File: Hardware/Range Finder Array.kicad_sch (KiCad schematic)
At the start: 8 parts

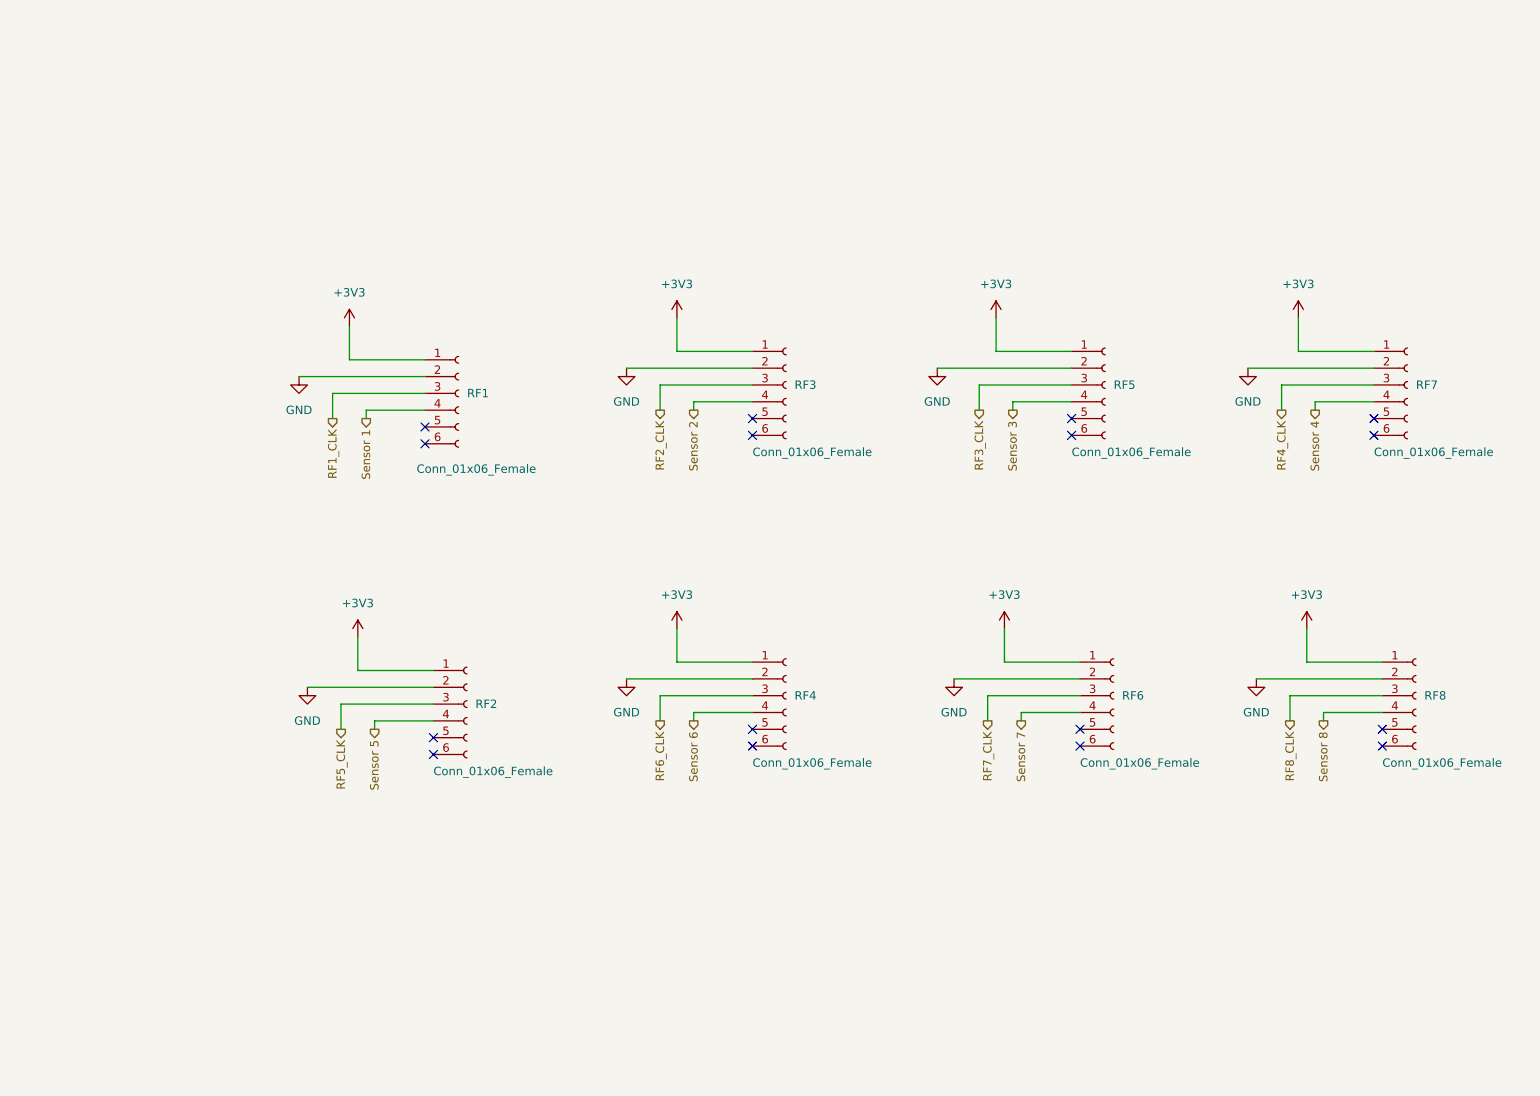
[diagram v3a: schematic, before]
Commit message: Add VL53L0X
Added VL53L0X range finders and reworked traces.
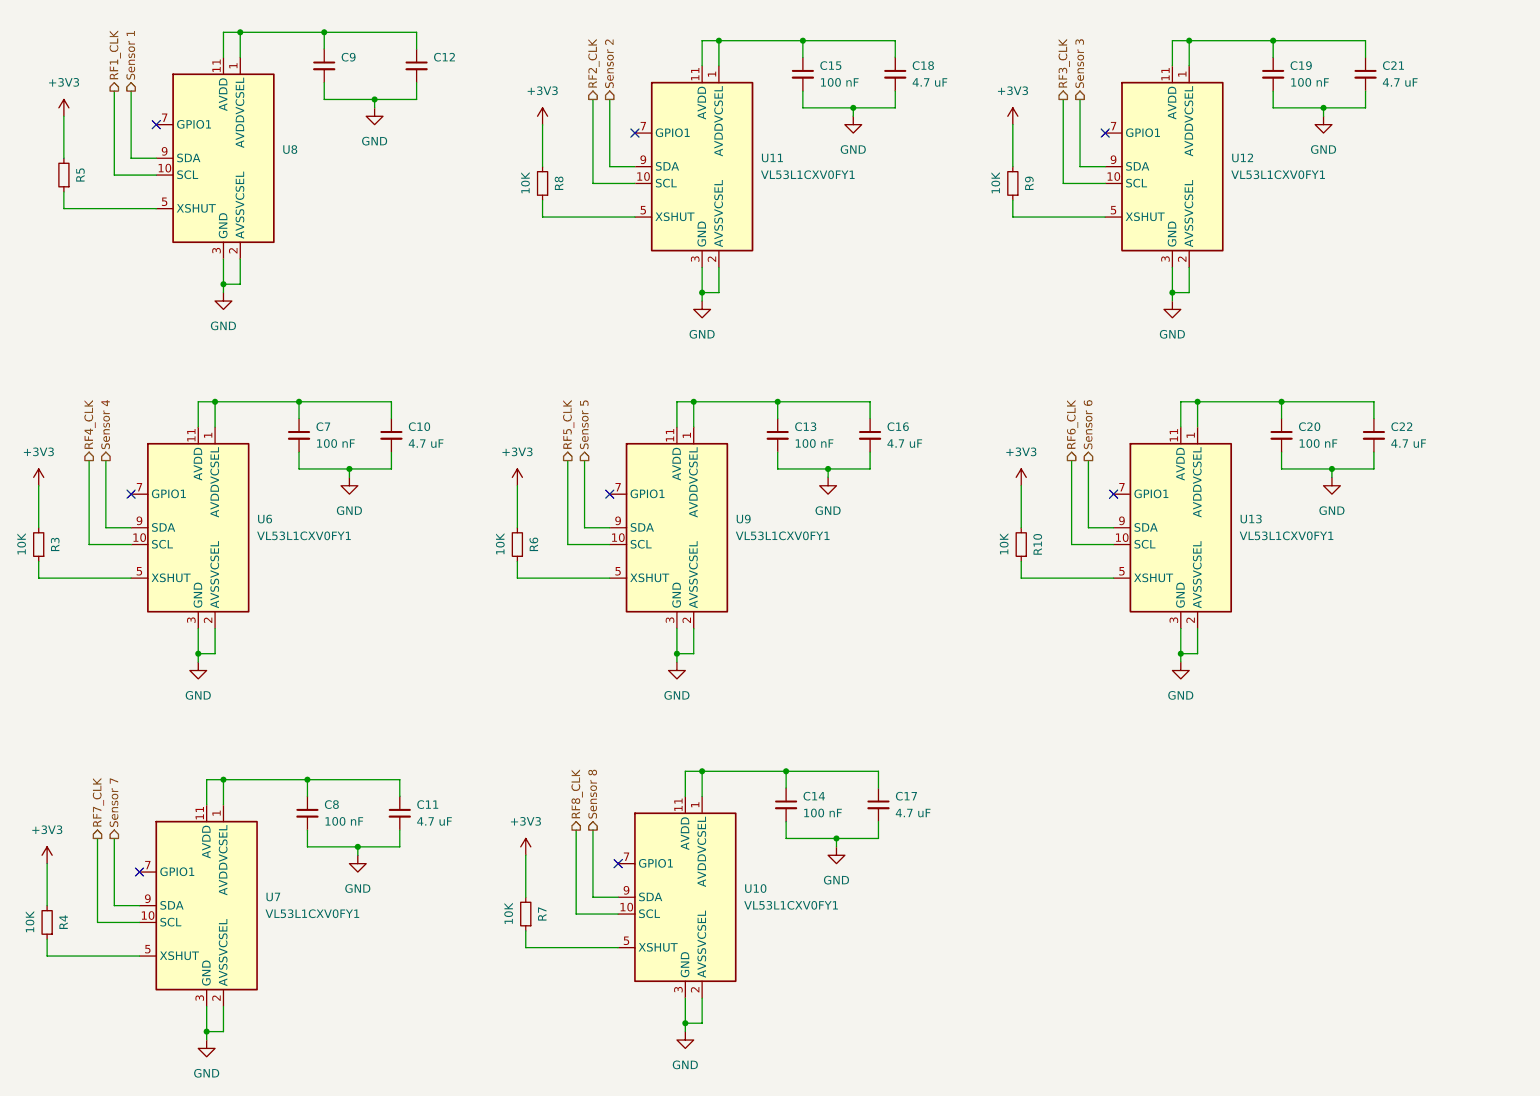
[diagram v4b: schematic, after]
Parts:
- removed RF1, RF2, RF3, RF4, RF5, RF6, RF7, RF8: Conn_01x06_Female, Connector_PinHeader_2.54mm:PinHeader_1x06_P2.54mm_Vertical, symbol Connector:Conn_01x06_Female
- added C10, C11, C16, C17, C18, C21, C22: 4.7 uF, Capacitor_SMD:C_0805_2012Metric, symbol Device:C_Small
- added C12, C9: (no value), symbol Device:C_Small
- added C13, C14, C15, C19, C20, C7, C8: 100 nF, Capacitor_SMD:C_0805_2012Metric, symbol Device:C_Small
- added R10, R3, R4, R6, R7, R8, R9: 10K, Resistor_SMD:R_0805_2012Metric, symbol Device:R_Small
- added R5: (no value), symbol Device:R_Small
- added U10, U11, U12, U13, U6, U7, U9: VL53L1CXV0FY1, Sensor_Distance:ST_VL53L1x, symbol Sensor_Distance:VL53L1CXV0FY1
- added U8: (no value), symbol Sensor_Distance:VL53L1CXV0FY1
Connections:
- net +3V3: now also R10.2, R3.2, R4.2, R5.2, R6.2, R7.2, R8.2, R9.2
- net GND: now also C10.2, C11.2, C12.2, C13.2, C14.2, C15.2, C16.2, C17.2, C18.2, C19.2, C20.2, C21.2, C22.2, C7.2, C8.2, C9.2, U10.12 (GND), U10.2 (AVSSVCSEL), U10.3 (GND), U10.4 (GND), U10.6 (GND), U11.12 (GND), U11.2 (AVSSVCSEL), U11.3 (GND), U11.4 (GND), U11.6 (GND), U12.12 (GND), U12.2 (AVSSVCSEL), U12.3 (GND), U12.4 (GND), U12.6 (GND), U13.12 (GND), U13.2 (AVSSVCSEL), U13.3 (GND), U13.4 (GND), U13.6 (GND), U6.12 (GND), U6.2 (AVSSVCSEL), U6.3 (GND), U6.4 (GND), U6.6 (GND), U7.12 (GND), U7.2 (AVSSVCSEL), U7.3 (GND), U7.4 (GND), U7.6 (GND), U8.12 (GND), U8.2 (AVSSVCSEL), U8.3 (GND), U8.4 (GND), U8.6 (GND), U9.12 (GND), U9.2 (AVSSVCSEL), U9.3 (GND), U9.4 (GND), U9.6 (GND)
- net RF1_CLK: now also U8.10 (SCL)
- net RF2_CLK: now also U11.10 (SCL)
- net RF3_CLK: now also U12.10 (SCL)
- net RF4_CLK: now also U6.10 (SCL)
- net RF5_CLK: now also U9.10 (SCL)
- net RF6_CLK: now also U13.10 (SCL)
- net RF7_CLK: now also U7.10 (SCL)
- net RF8_CLK: now also U10.10 (SCL)
- net Sensor 1: now also U8.9 (SDA)
- net Sensor 2: now also U11.9 (SDA)
- net Sensor 3: now also U12.9 (SDA)
- net Sensor 4: now also U6.9 (SDA)
- net Sensor 5: now also U9.9 (SDA)
- net Sensor 6: now also U13.9 (SDA)
- net Sensor 7: now also U7.9 (SDA)
- net Sensor 8: now also U10.9 (SDA)
- new net: C14.1, C17.1, U10.1 (AVDDVCSEL), U10.11 (AVDD)
- new net: C15.1, C18.1, U11.1 (AVDDVCSEL), U11.11 (AVDD)
- new net: C19.1, C21.1, U12.1 (AVDDVCSEL), U12.11 (AVDD)
- new net: C13.1, C16.1, U9.1 (AVDDVCSEL), U9.11 (AVDD)
- new net: C12.1, C9.1, U8.1 (AVDDVCSEL), U8.11 (AVDD)
- new net: R7.1, U10.5 (XSHUT)
- new net: C11.1, C8.1, U7.1 (AVDDVCSEL), U7.11 (AVDD)
- new net: R8.1, U11.5 (XSHUT)
- new net: C10.1, C7.1, U6.1 (AVDDVCSEL), U6.11 (AVDD)
- new net: R3.1, U6.5 (XSHUT)
- new net: C20.1, C22.1, U13.1 (AVDDVCSEL), U13.11 (AVDD)
- new net: R10.1, U13.5 (XSHUT)
- new net: R9.1, U12.5 (XSHUT)
- new net: R4.1, U7.5 (XSHUT)
- new net: R6.1, U9.5 (XSHUT)
- new net: R5.1, U8.5 (XSHUT)
- no-connect marks 16 -> 8

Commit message: Everything Changes
Lets Fix it.
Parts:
- C10, C11, C16, C17, C18, C21, C22: value 4.7 uF -> (none); footprint Capacitor_SMD:C_0805_2012Metric -> (none)
- C13, C14, C15, C19, C20, C7, C8: value 100 nF -> (none); footprint Capacitor_SMD:C_0805_2012Metric -> (none)
- U8: value (none) -> VL53L1CXV0FY1; footprint (none) -> Sensor_Distance:ST_VL53L1x
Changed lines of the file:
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@@
       (effects (font (size 1.27 1.27)) (justify left))
     )
-    (property "Value" "100 nF" (id 1) (at 142.24 146.0562 0)
-      (effects (font (size 1.27 1.27)) (justify left))
-    )
-    (property "Footprint" "Capacitor_SMD:C_0805_2012Metric" (id 2) (at 139.7 144.78 0)
+    (property "Value" "" (id 1) (at 142.24 146.0562 0)
+      (effects (font (size 1.27 1.27)) (justify left))
+    )
+    (property "Footprint" "" (id 2) (at 139.7 144.78 0)
       (effects (font (size 1.27 1.27)) hide)
     )
@@
       (effects (font (size 1.27 1.27)) (justify left))
     )
-    (property "Value" "100 nF" (id 1) (at 144.78 35.5662 0)
-      (effects (font (size 1.27 1.27)) (justify left))
-    )
-    (property "Footprint" "Capacitor_SMD:C_0805_2012Metric" (id 2) (at 142.24 34.29 0)
+    (property "Value" "" (id 1) (at 144.78 35.5662 0)
+      (effects (font (size 1.27 1.27)) (justify left))
+    )
+    (property "Footprint" "" (id 2) (at 142.24 34.29 0)
       (effects (font (size 1.27 1.27)) hide)
     )
@@
       (effects (font (size 1.27 1.27)) (justify left))
     )
-    (property "Value" "4.7 uF" (id 1) (at 229.87 35.5662 0)
-      (effects (font (size 1.27 1.27)) (justify left))
-    )
-    (property "Footprint" "Capacitor_SMD:C_0805_2012Metric" (id 2) (at 227.33 34.29 0)
+    (property "Value" "" (id 1) (at 229.87 35.5662 0)
+      (effects (font (size 1.27 1.27)) (justify left))
+    )
+    (property "Footprint" "" (id 2) (at 227.33 34.29 0)
       (effects (font (size 1.27 1.27)) hide)
     )
@@
       (effects (font (size 1.27 1.27)) (justify left))
     )
-    (property "Value" "4.7 uF" (id 1) (at 156.21 146.0562 0)
-      (effects (font (size 1.27 1.27)) (justify left))
-    )
-    (property "Footprint" "Capacitor_SMD:C_0805_2012Metric" (id 2) (at 153.67 144.78 0)
+    (property "Value" "" (id 1) (at 156.21 146.0562 0)
+      (effects (font (size 1.27 1.27)) (justify left))
+    )
+    (property "Footprint" "" (id 2) (at 153.67 144.78 0)
       (effects (font (size 1.27 1.27)) hide)
     )
@@
       (effects (font (size 1.27 1.27)) (justify left))
     )
-    (property "Value" "4.7 uF" (id 1) (at 154.94 90.1762 0)
-      (effects (font (size 1.27 1.27)) (justify left))
-    )
-    (property "Footprint" "Capacitor_SMD:C_0805_2012Metric" (id 2) (at 152.4 88.9 0)
+    (property "Value" "" (id 1) (at 154.94 90.1762 0)
+      (effects (font (size 1.27 1.27)) (justify left))
+    )
+    (property "Footprint" "" (id 2) (at 152.4 88.9 0)
       (effects (font (size 1.27 1.27)) hide)
     )
@@
       (effects (font (size 1.27 1.27)) (justify left))
     )
-    (property "Value" "100 nF" (id 1) (at 215.9 35.5662 0)
-      (effects (font (size 1.27 1.27)) (justify left))
-    )
-    (property "Footprint" "Capacitor_SMD:C_0805_2012Metric" (id 2) (at 213.36 34.29 0)
+    (property "Value" "" (id 1) (at 215.9 35.5662 0)
+      (effects (font (size 1.27 1.27)) (justify left))
+    )
+    (property "Footprint" "" (id 2) (at 213.36 34.29 0)
       (effects (font (size 1.27 1.27)) hide)
     )
@@
       (effects (font (size 1.27 1.27)) (justify left))
     )
-    (property "Value" "4.7 uF" (id 1) (at 83.82 147.3262 0)
-      (effects (font (size 1.27 1.27)) (justify left))
-    )
-    (property "Footprint" "Capacitor_SMD:C_0805_2012Metric" (id 2) (at 81.28 146.05 0)
+    (property "Value" "" (id 1) (at 83.82 147.3262 0)
+      (effects (font (size 1.27 1.27)) (justify left))
+    )
+    (property "Footprint" "" (id 2) (at 81.28 146.05 0)
       (effects (font (size 1.27 1.27)) hide)
     )
@@
       (effects (font (size 1.27 1.27)) (justify left))
     )
-    (property "Value" "100 nF" (id 1) (at 69.85 147.3262 0)
-      (effects (font (size 1.27 1.27)) (justify left))
-    )
-    (property "Footprint" "Capacitor_SMD:C_0805_2012Metric" (id 2) (at 67.31 146.05 0)
+    (property "Value" "" (id 1) (at 69.85 147.3262 0)
+      (effects (font (size 1.27 1.27)) (justify left))
+    )
+    (property "Footprint" "" (id 2) (at 67.31 146.05 0)
       (effects (font (size 1.27 1.27)) hide)
     )
@@
       (effects (font (size 1.27 1.27)) (justify left))
     )
-    (property "Value" "100 nF" (id 1) (at 140.97 90.1762 0)
-      (effects (font (size 1.27 1.27)) (justify left))
-    )
-    (property "Footprint" "Capacitor_SMD:C_0805_2012Metric" (id 2) (at 138.43 88.9 0)
+    (property "Value" "" (id 1) (at 140.97 90.1762 0)
+      (effects (font (size 1.27 1.27)) (justify left))
+    )
+    (property "Footprint" "" (id 2) (at 138.43 88.9 0)
       (effects (font (size 1.27 1.27)) hide)
     )
@@
       (effects (font (size 1.27 1.27)) (justify left))
     )
-    (property "Value" "4.7 uF" (id 1) (at 158.75 35.5662 0)
-      (effects (font (size 1.27 1.27)) (justify left))
-    )
-    (property "Footprint" "Capacitor_SMD:C_0805_2012Metric" (id 2) (at 156.21 34.29 0)
+    (property "Value" "" (id 1) (at 158.75 35.5662 0)
+      (effects (font (size 1.27 1.27)) (justify left))
+    )
+    (property "Footprint" "" (id 2) (at 156.21 34.29 0)
       (effects (font (size 1.27 1.27)) hide)
     )
@@
       (effects (font (size 1.27 1.27)) (justify left))
     )
-    (property "Value" "100 nF" (id 1) (at 217.17 90.1762 0)
-      (effects (font (size 1.27 1.27)) (justify left))
-    )
-    (property "Footprint" "Capacitor_SMD:C_0805_2012Metric" (id 2) (at 214.63 88.9 0)
+    (property "Value" "" (id 1) (at 217.17 90.1762 0)
+      (effects (font (size 1.27 1.27)) (justify left))
+    )
+    (property "Footprint" "" (id 2) (at 214.63 88.9 0)
       (effects (font (size 1.27 1.27)) hide)
     )
@@
       (effects (font (size 1.27 1.27)) (justify left))
     )
-    (property "Value" "100 nF" (id 1) (at 68.58 90.1762 0)
-      (effects (font (size 1.27 1.27)) (justify left))
-    )
-    (property "Footprint" "Capacitor_SMD:C_0805_2012Metric" (id 2) (at 66.04 88.9 0)
+    (property "Value" "" (id 1) (at 68.58 90.1762 0)
+      (effects (font (size 1.27 1.27)) (justify left))
+    )
+    (property "Footprint" "" (id 2) (at 66.04 88.9 0)
       (effects (font (size 1.27 1.27)) hide)
     )
@@
       (effects (font (size 1.27 1.27)) (justify left))
     )
-    (property "Value" "4.7 uF" (id 1) (at 231.14 90.1762 0)
-      (effects (font (size 1.27 1.27)) (justify left))
-    )
-    (property "Footprint" "Capacitor_SMD:C_0805_2012Metric" (id 2) (at 228.6 88.9 0)
+    (property "Value" "" (id 1) (at 231.14 90.1762 0)
+      (effects (font (size 1.27 1.27)) (justify left))
+    )
+    (property "Footprint" "" (id 2) (at 228.6 88.9 0)
       (effects (font (size 1.27 1.27)) hide)
     )
@@
       (effects (font (size 1.27 1.27)) (justify left))
     )
-    (property "Value" "4.7 uF" (id 1) (at 82.55 90.1762 0)
-      (effects (font (size 1.27 1.27)) (justify left))
-    )
-    (property "Footprint" "Capacitor_SMD:C_0805_2012Metric" (id 2) (at 80.01 88.9 0)
+    (property "Value" "" (id 1) (at 82.55 90.1762 0)
+      (effects (font (size 1.27 1.27)) (justify left))
+    )
+    (property "Footprint" "" (id 2) (at 80.01 88.9 0)
       (effects (font (size 1.27 1.27)) hide)
     )
@@
       (effects (font (size 1.27 1.27)) (justify left))
     )
-    (property "Value" "" (id 1) (at 63.5 48.2599 0)
-      (effects (font (size 1.27 1.27)) (justify left))
-    )
-    (property "Footprint" "" (id 2) (at 71.755 60.96 0)
-      (effects (font (size 1.27 1.27)) hide)
-    )
+    (property "Value" "VL53L1CXV0FY1" (id 1) (at 63.5 48.2599 0)
+      (effects (font (size 1.27 1.27)) (justify left))
+    )
+    (property "Footprint" "Sensor_Distance:ST_VL53L1x" (id 2) (at 71.755 60.96 0)
+      (effects (font (size 1.27 1.27)) hide)
+    )
